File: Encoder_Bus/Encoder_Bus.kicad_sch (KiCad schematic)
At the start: 26 parts, among them J1 Bonn_01x04, J10 Bonn_01x07, J11 Bonn_01x04, J12 Bonn_01x04, J13 Bonn_01x04, J14 Bonn_01x04, J15 Bonn_01x04, J16 Bonn_01x04, J17 Bonn_01x04, J18 Bonn_01x04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

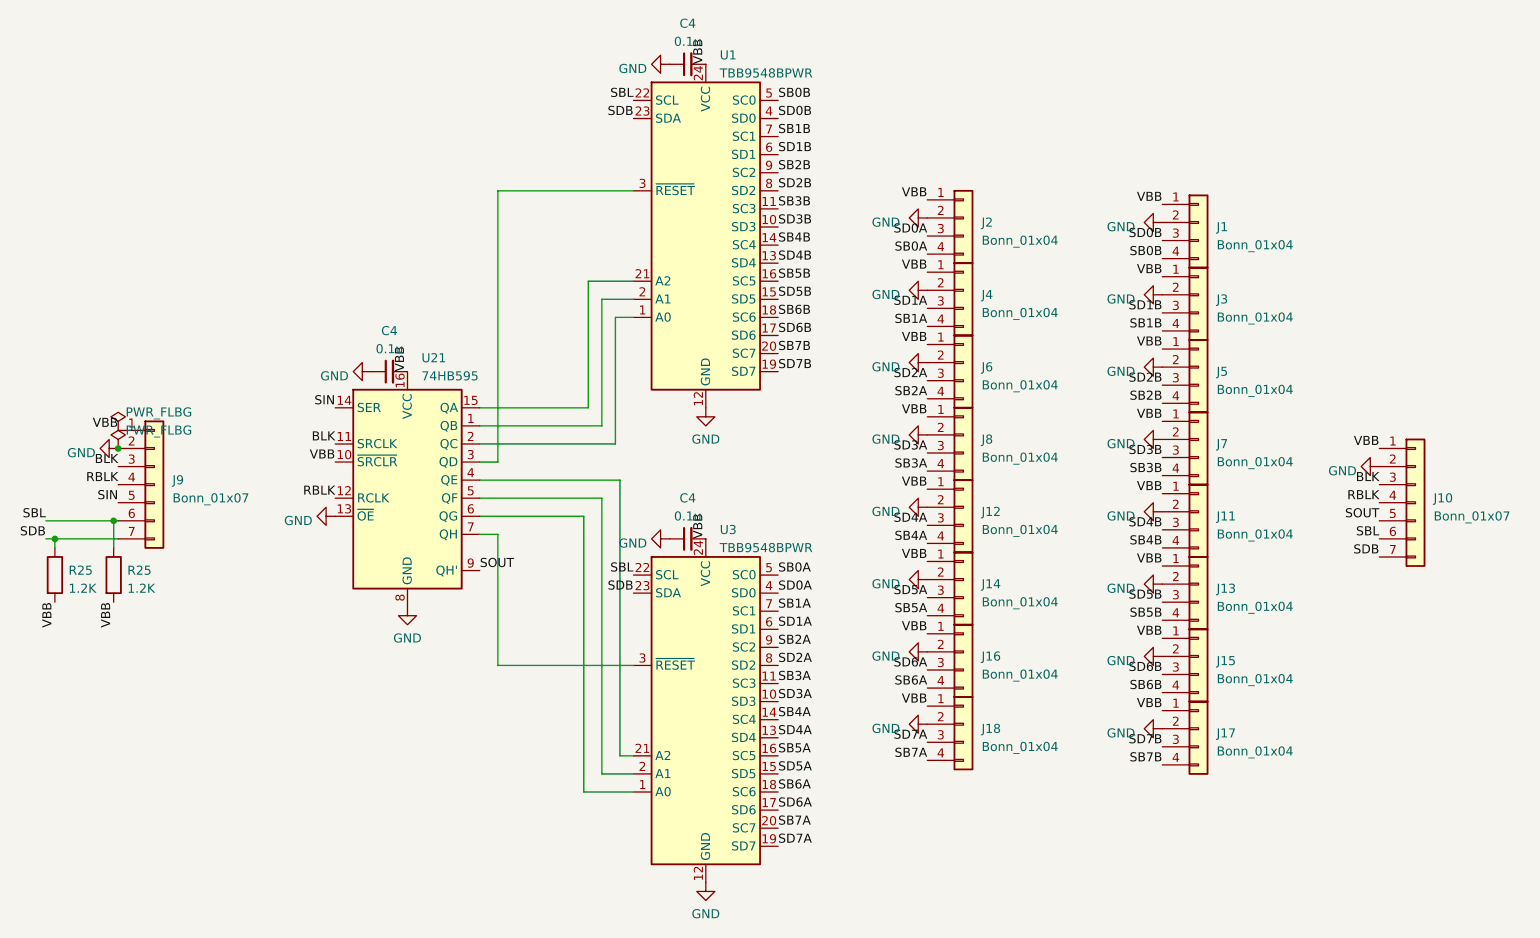
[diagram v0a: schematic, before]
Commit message: Fixed some silkscreen stuff, started DRIFT bus layout
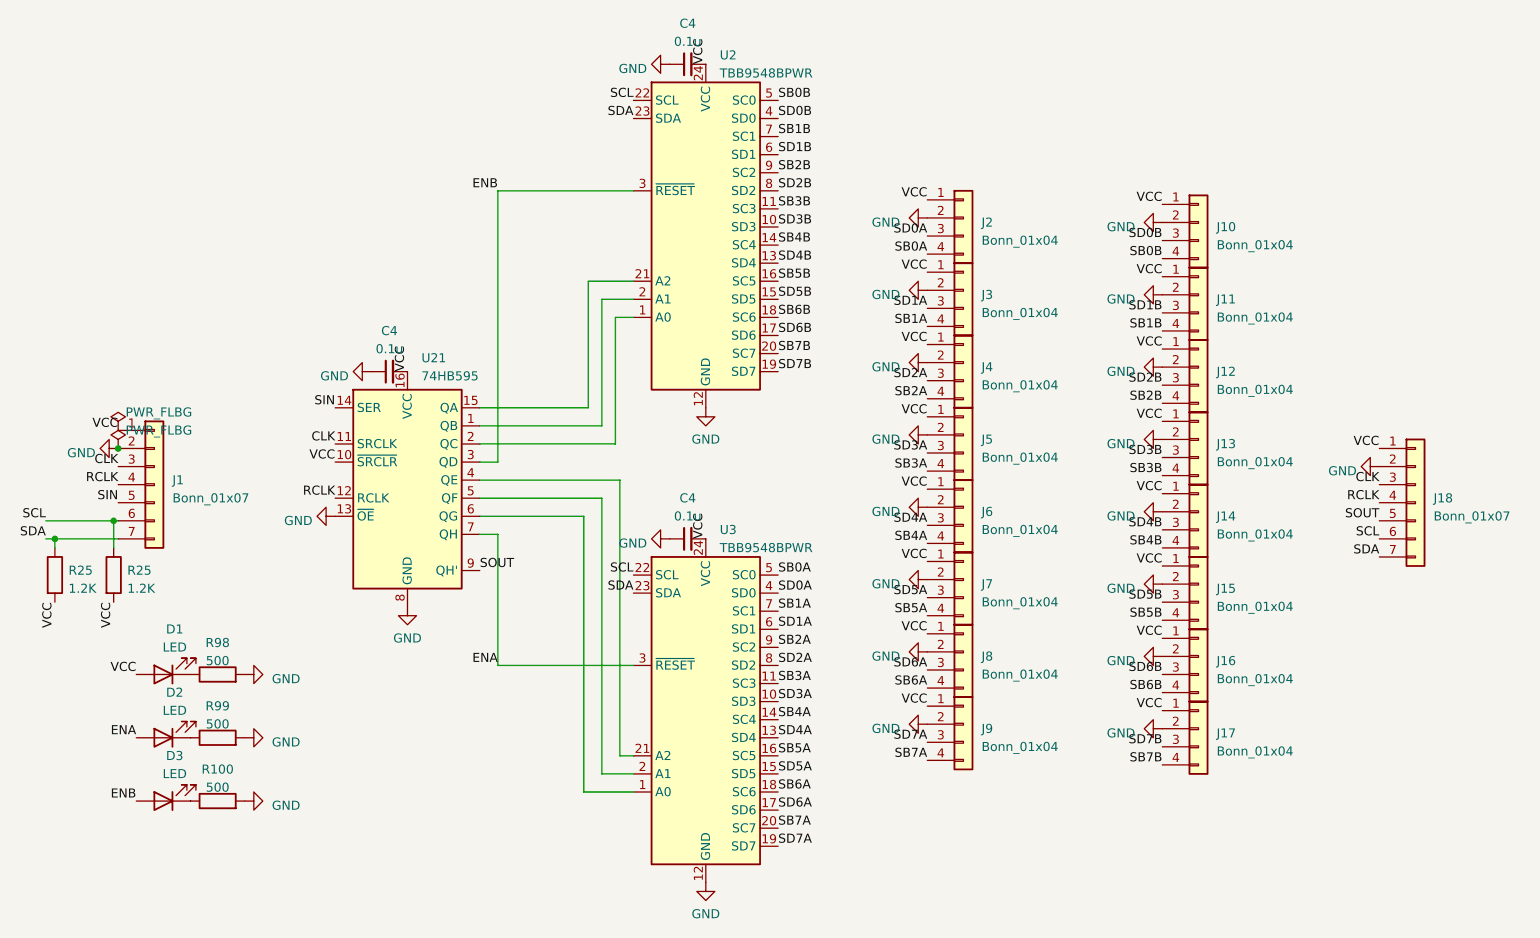
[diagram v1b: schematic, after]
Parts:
- added D1, D2, D3: LED, LED_SMD:LED_0603_1608Metric, symbol Device:LED
- added R100, R98, R99: 500, Resistor_SMD:R_0402_1005Metric, symbol Device:R
- J1: renamed from J9; footprint (none) -> Connector_PinHeader_2.54mm:PinHeader_1x07_P2.54mm_Vertical
- J10: renamed from J1; footprint (none) -> Connector_PinHeader_2.54mm:PinHeader_1x04_P2.54mm_Vertical
- J11: renamed from J3; footprint (none) -> Connector_PinHeader_2.54mm:PinHeader_1x04_P2.54mm_Vertical
- J12: renamed from J5; footprint (none) -> Connector_PinHeader_2.54mm:PinHeader_1x04_P2.54mm_Vertical
- J13: renamed from J7; footprint (none) -> Connector_PinHeader_2.54mm:PinHeader_1x04_P2.54mm_Vertical
- J14: renamed from J11; footprint (none) -> Connector_PinHeader_2.54mm:PinHeader_1x04_P2.54mm_Vertical
- J15: renamed from J13; footprint (none) -> Connector_PinHeader_2.54mm:PinHeader_1x04_P2.54mm_Vertical
- J16: renamed from J15; footprint (none) -> Connector_PinHeader_2.54mm:PinHeader_1x04_P2.54mm_Vertical
- J17, J2: footprint (none) -> Connector_PinHeader_2.54mm:PinHeader_1x04_P2.54mm_Vertical
- J18: renamed from J10; footprint (none) -> Connector_PinHeader_2.54mm:PinHeader_1x07_P2.54mm_Vertical
- J3: renamed from J4; footprint (none) -> Connector_PinHeader_2.54mm:PinHeader_1x04_P2.54mm_Vertical
- J4: renamed from J6; footprint (none) -> Connector_PinHeader_2.54mm:PinHeader_1x04_P2.54mm_Vertical
- J5: renamed from J8; footprint (none) -> Connector_PinHeader_2.54mm:PinHeader_1x04_P2.54mm_Vertical
- J6: renamed from J12; footprint (none) -> Connector_PinHeader_2.54mm:PinHeader_1x04_P2.54mm_Vertical
- J7: renamed from J14; footprint (none) -> Connector_PinHeader_2.54mm:PinHeader_1x04_P2.54mm_Vertical
- J8: renamed from J16; footprint (none) -> Connector_PinHeader_2.54mm:PinHeader_1x04_P2.54mm_Vertical
- J9: renamed from J18; footprint (none) -> Connector_PinHeader_2.54mm:PinHeader_1x04_P2.54mm_Vertical
- renumbered U1 to U2
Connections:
- net GND: now also R100.2, R98.2, R99.2
- net ENB: now reaches U2.3 (~{RESET}), U21.3 (QD)
- net ENB: now also D3.2 (A)
- net ENA: now reaches U21.7 (QH), U3.3 (~{RESET})
- net ENA: now also D2.2 (A)
- net BLK renamed CLK
- net RBLK renamed RCLK
- net SBL renamed SCL
- net SDB renamed SDA
- net VBB renamed VCC
- net VCC: now also D1.2 (A)
- new net: D2.1 (K), R99.1
- new net: D1.1 (K), R98.1
- new net: D3.1 (K), R100.1
